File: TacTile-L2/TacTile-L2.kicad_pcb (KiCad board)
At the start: 2 copper layers, 25 x 60 mm, 11 parts, among them J1 Conn_01x05, J2 Conn_01x05, U1 74HC595

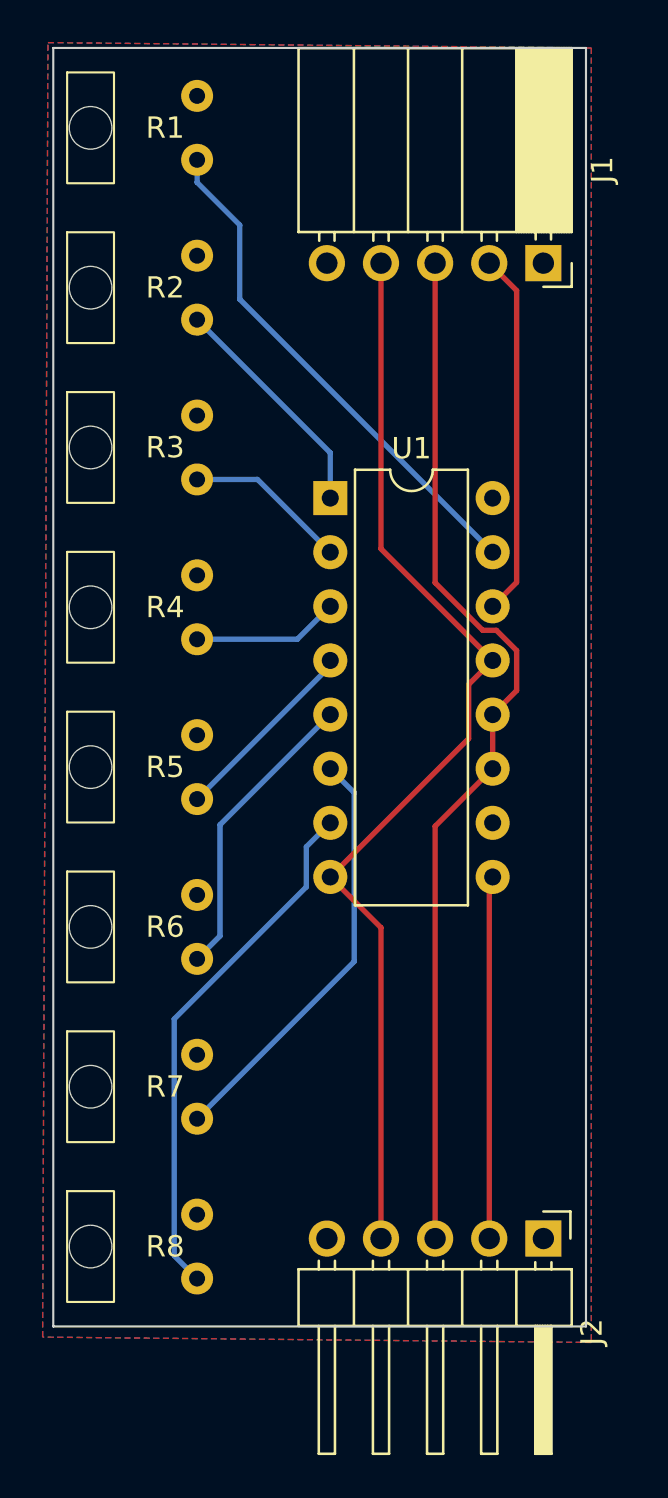
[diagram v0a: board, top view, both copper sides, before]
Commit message: Adjusted mounting for laser boards
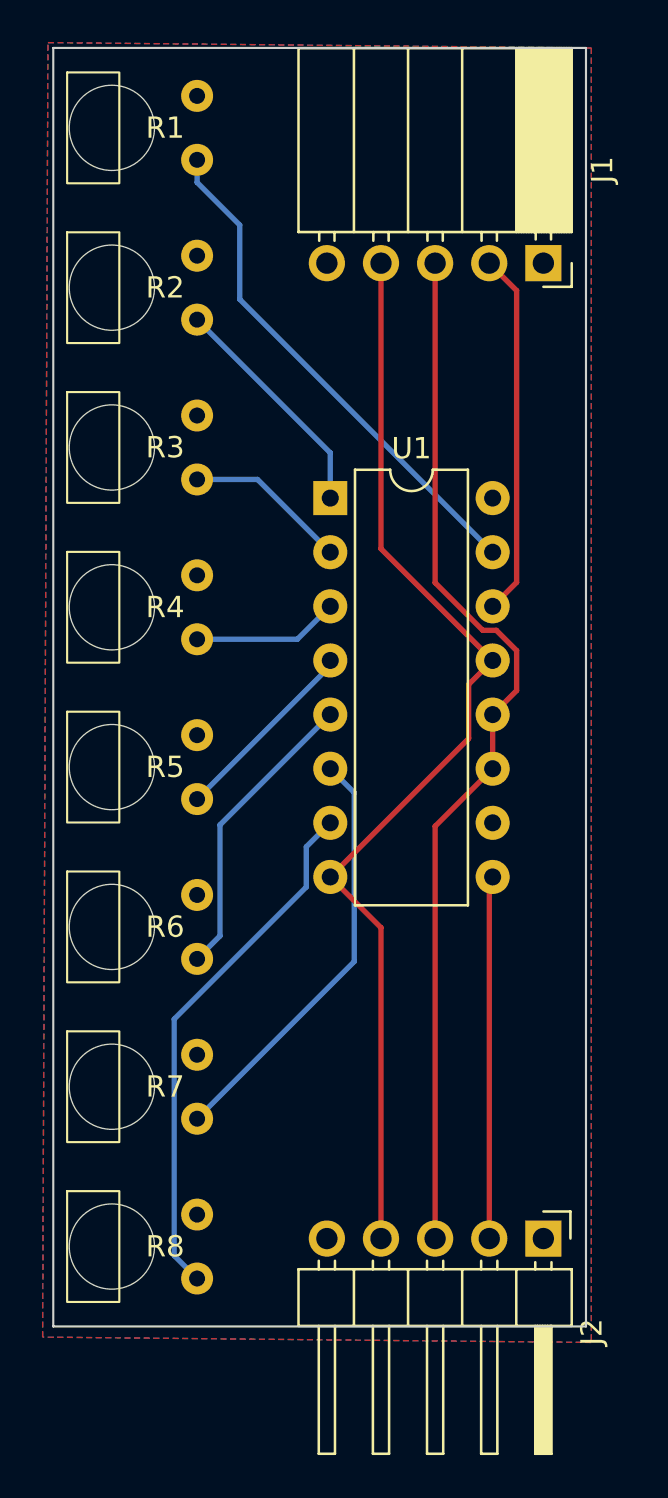
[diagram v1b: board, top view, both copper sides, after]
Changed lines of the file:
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@@
         (effects (font (size 1 1) (thickness 0.15)))
     )
-    (fp_rect (start -1.1 -2.6) (end 1.1 2.6)
-      (stroke (width 0.1) (type default)) (fill none) (layer "F.SilkS"))
-    (fp_rect (start -1.5 -3.75) (end 3 3.75)
-      (stroke (width 0.05) (type default)) (fill none) (layer "F.CrtYd"))
-    (fp_rect (start -1 -2.5) (end 1 2.5)
-      (stroke (width 0.1) (type default)) (fill none) (layer "F.Fab"))
-    (pad "" np_thru_hole circle (at 0 0) (size 2 2) (drill 2) (layers "F&B.Cu" "*.Mask"))
+    (fp_rect (start -1.1 -2.6) (end 1.35 2.6)
+      (stroke (width 0.1) (type default)) (fill none) (layer "F.SilkS"))
+    (fp_rect (start -1 -3.75) (end 3 3.75)
+      (stroke (width 0.05) (type default)) (fill none) (layer "F.CrtYd"))
+    (fp_rect (start -1 -2.5) (end 1.25 2.5)
+      (stroke (width 0.1) (type default)) (fill none) (layer "F.Fab"))
+    (pad "" np_thru_hole circle (at 1 0) (size 4 4) (drill 4) (layers "F&B.Cu" "*.Mask" "B.SilkS"))
     (pad "1" thru_hole circle (at 5 -1.5) (size 1.5 1.5) (drill 0.75) (layers "*.Cu" "*.Mask")
       (net 5 "/OUT") (pintype "passive"))
@@
         (effects (font (size 1 1) (thickness 0.15)))
     )
-    (fp_rect (start -1.1 -2.6) (end 1.1 2.6)
-      (stroke (width 0.1) (type default)) (fill none) (layer "F.SilkS"))
-    (fp_rect (start -1.5 -3.75) (end 3 3.75)
-      (stroke (width 0.05) (type default)) (fill none) (layer "F.CrtYd"))
-    (fp_rect (start -1 -2.5) (end 1 2.5)
-      (stroke (width 0.1) (type default)) (fill none) (layer "F.Fab"))
-    (pad "" np_thru_hole circle (at 0 0) (size 2 2) (drill 2) (layers "F&B.Cu" "*.Mask"))
+    (fp_rect (start -1.1 -2.6) (end 1.35 2.6)
+      (stroke (width 0.1) (type default)) (fill none) (layer "F.SilkS"))
+    (fp_rect (start -1 -3.75) (end 3 3.75)
+      (stroke (width 0.05) (type default)) (fill none) (layer "F.CrtYd"))
+    (fp_rect (start -1 -2.5) (end 1.25 2.5)
+      (stroke (width 0.1) (type default)) (fill none) (layer "F.Fab"))
+    (pad "" np_thru_hole circle (at 1 0) (size 4 4) (drill 4) (layers "F&B.Cu" "*.Mask" "B.SilkS"))
     (pad "1" thru_hole circle (at 5 -1.5) (size 1.5 1.5) (drill 0.75) (layers "*.Cu" "*.Mask")
       (net 5 "/OUT") (pintype "passive"))
@@
         (effects (font (size 1 1) (thickness 0.15)))
     )
-    (fp_rect (start -1.1 -2.6) (end 1.1 2.6)
-      (stroke (width 0.1) (type default)) (fill none) (layer "F.SilkS"))
-    (fp_rect (start -1.5 -3.75) (end 3 3.75)
-      (stroke (width 0.05) (type default)) (fill none) (layer "F.CrtYd"))
-    (fp_rect (start -1 -2.5) (end 1 2.5)
-      (stroke (width 0.1) (type default)) (fill none) (layer "F.Fab"))
-    (pad "" np_thru_hole circle (at 0 0) (size 2 2) (drill 2) (layers "F&B.Cu" "*.Mask"))
+    (fp_rect (start -1.1 -2.6) (end 1.35 2.6)
+      (stroke (width 0.1) (type default)) (fill none) (layer "F.SilkS"))
+    (fp_rect (start -1 -3.75) (end 3 3.75)
+      (stroke (width 0.05) (type default)) (fill none) (layer "F.CrtYd"))
+    (fp_rect (start -1 -2.5) (end 1.25 2.5)
+      (stroke (width 0.1) (type default)) (fill none) (layer "F.Fab"))
+    (pad "" np_thru_hole circle (at 1 0) (size 4 4) (drill 4) (layers "F&B.Cu" "*.Mask" "B.SilkS"))
     (pad "1" thru_hole circle (at 5 -1.5) (size 1.5 1.5) (drill 0.75) (layers "*.Cu" "*.Mask")
       (net 5 "/OUT") (pintype "passive"))
@@
         (effects (font (size 1 1) (thickness 0.15)))
     )
-    (fp_rect (start -1.1 -2.6) (end 1.1 2.6)
-      (stroke (width 0.1) (type default)) (fill none) (layer "F.SilkS"))
-    (fp_rect (start -1.5 -3.75) (end 3 3.75)
-      (stroke (width 0.05) (type default)) (fill none) (layer "F.CrtYd"))
-    (fp_rect (start -1 -2.5) (end 1 2.5)
-      (stroke (width 0.1) (type default)) (fill none) (layer "F.Fab"))
-    (pad "" np_thru_hole circle (at 0 0) (size 2 2) (drill 2) (layers "F&B.Cu" "*.Mask"))
+    (fp_rect (start -1.1 -2.6) (end 1.35 2.6)
+      (stroke (width 0.1) (type default)) (fill none) (layer "F.SilkS"))
+    (fp_rect (start -1 -3.75) (end 3 3.75)
+      (stroke (width 0.05) (type default)) (fill none) (layer "F.CrtYd"))
+    (fp_rect (start -1 -2.5) (end 1.25 2.5)
+      (stroke (width 0.1) (type default)) (fill none) (layer "F.Fab"))
+    (pad "" np_thru_hole circle (at 1 0) (size 4 4) (drill 4) (layers "F&B.Cu" "*.Mask" "B.SilkS"))
     (pad "1" thru_hole circle (at 5 -1.5) (size 1.5 1.5) (drill 0.75) (layers "*.Cu" "*.Mask")
       (net 5 "/OUT") (pintype "passive"))
@@
         (effects (font (size 1 1) (thickness 0.15)))
     )
-    (fp_rect (start -1.1 -2.6) (end 1.1 2.6)
-      (stroke (width 0.1) (type default)) (fill none) (layer "F.SilkS"))
-    (fp_rect (start -1.5 -3.75) (end 3 3.75)
-      (stroke (width 0.05) (type default)) (fill none) (layer "F.CrtYd"))
-    (fp_rect (start -1 -2.5) (end 1 2.5)
-      (stroke (width 0.1) (type default)) (fill none) (layer "F.Fab"))
-    (pad "" np_thru_hole circle (at 0 0) (size 2 2) (drill 2) (layers "F&B.Cu" "*.Mask"))
+    (fp_rect (start -1.1 -2.6) (end 1.35 2.6)
+      (stroke (width 0.1) (type default)) (fill none) (layer "F.SilkS"))
+    (fp_rect (start -1 -3.75) (end 3 3.75)
+      (stroke (width 0.05) (type default)) (fill none) (layer "F.CrtYd"))
+    (fp_rect (start -1 -2.5) (end 1.25 2.5)
+      (stroke (width 0.1) (type default)) (fill none) (layer "F.Fab"))
+    (pad "" np_thru_hole circle (at 1 0) (size 4 4) (drill 4) (layers "F&B.Cu" "*.Mask" "B.SilkS"))
     (pad "1" thru_hole circle (at 5 -1.5) (size 1.5 1.5) (drill 0.75) (layers "*.Cu" "*.Mask")
       (net 5 "/OUT") (pintype "passive"))
@@
         (effects (font (size 1 1) (thickness 0.15)))
     )
-    (fp_rect (start -1.1 -2.6) (end 1.1 2.6)
-      (stroke (width 0.1) (type default)) (fill none) (layer "F.SilkS"))
-    (fp_rect (start -1.5 -3.75) (end 3 3.75)
-      (stroke (width 0.05) (type default)) (fill none) (layer "F.CrtYd"))
-    (fp_rect (start -1 -2.5) (end 1 2.5)
-      (stroke (width 0.1) (type default)) (fill none) (layer "F.Fab"))
-    (pad "" np_thru_hole circle (at 0 0) (size 2 2) (drill 2) (layers "F&B.Cu" "*.Mask"))
+    (fp_rect (start -1.1 -2.6) (end 1.35 2.6)
+      (stroke (width 0.1) (type default)) (fill none) (layer "F.SilkS"))
+    (fp_rect (start -1 -3.75) (end 3 3.75)
+      (stroke (width 0.05) (type default)) (fill none) (layer "F.CrtYd"))
+    (fp_rect (start -1 -2.5) (end 1.25 2.5)
+      (stroke (width 0.1) (type default)) (fill none) (layer "F.Fab"))
+    (pad "" np_thru_hole circle (at 1 0) (size 4 4) (drill 4) (layers "F&B.Cu" "*.Mask" "B.SilkS"))
     (pad "1" thru_hole circle (at 5 -1.5) (size 1.5 1.5) (drill 0.75) (layers "*.Cu" "*.Mask")
       (net 5 "/OUT") (pintype "passive"))
@@
         (effects (font (size 1 1) (thickness 0.15)))
     )
-    (fp_rect (start -1.1 -2.6) (end 1.1 2.6)
-      (stroke (width 0.1) (type default)) (fill none) (layer "F.SilkS"))
-    (fp_rect (start -1.5 -3.75) (end 3 3.75)
-      (stroke (width 0.05) (type default)) (fill none) (layer "F.CrtYd"))
-    (fp_rect (start -1 -2.5) (end 1 2.5)
-      (stroke (width 0.1) (type default)) (fill none) (layer "F.Fab"))
-    (pad "" np_thru_hole circle (at 0 0) (size 2 2) (drill 2) (layers "F&B.Cu" "*.Mask"))
+    (fp_rect (start -1.1 -2.6) (end 1.35 2.6)
+      (stroke (width 0.1) (type default)) (fill none) (layer "F.SilkS"))
+    (fp_rect (start -1 -3.75) (end 3 3.75)
+      (stroke (width 0.05) (type default)) (fill none) (layer "F.CrtYd"))
+    (fp_rect (start -1 -2.5) (end 1.25 2.5)
+      (stroke (width 0.1) (type default)) (fill none) (layer "F.Fab"))
+    (pad "" np_thru_hole circle (at 1 0) (size 4 4) (drill 4) (layers "F&B.Cu" "*.Mask" "B.SilkS"))
     (pad "1" thru_hole circle (at 5 -1.5) (size 1.5 1.5) (drill 0.75) (layers "*.Cu" "*.Mask")
       (net 5 "/OUT") (pintype "passive"))
@@
         (effects (font (size 1 1) (thickness 0.15)))
     )
-    (fp_rect (start -1.1 -2.6) (end 1.1 2.6)
-      (stroke (width 0.1) (type default)) (fill none) (layer "F.SilkS"))
-    (fp_rect (start -1.5 -3.75) (end 3 3.75)
-      (stroke (width 0.05) (type default)) (fill none) (layer "F.CrtYd"))
-    (fp_rect (start -1 -2.5) (end 1 2.5)
-      (stroke (width 0.1) (type default)) (fill none) (layer "F.Fab"))
-    (pad "" np_thru_hole circle (at 0 0) (size 2 2) (drill 2) (layers "F&B.Cu" "*.Mask"))
-    (pad "1" thru_hole circle (at 5 -1.5) (size 1.5 1.5) (drill 0.75) (layers "*.Cu" "*.Mask")
-      (net 5 "/OUT") (pintype "passive"))
+    (fp_rect (start -1.1 -2.6) (end 1.35 2.6)
+      (stroke (width 0.1) (type default)) (fill none) (layer "F.SilkS"))
+    (fp_rect (start -1 -3.75) (end 3 3.75)
+      (stroke (width 0.05) (type default)) (fill none) (layer "F.CrtYd"))
+    (fp_rect (start -1 -2.5) (end 1.25 2.5)
+      (stroke (width 0.1) (type default)) (fill none) (layer "F.Fab"))
+    (pad "" np_thru_hole circle (at 1 0) (size 4 4) (drill 4) (layers "F&B.Cu" "*.Mask" "B.SilkS"))
+    (pad "1" thru_hole circle (at 5 -1.5) (size 1.5 1.5) (drill 0.75) (layers "*.Cu" "*.Mask")
+      (net 5 "/OUT") (pintype "passive"))
